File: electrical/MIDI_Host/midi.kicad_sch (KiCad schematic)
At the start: 35 parts, among them U1 BL1551B, U2 BL1551B, U3 BL1551B, U4 BL1551B, U5 74HC1G14GV, U6 6N137, U7 6N137

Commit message: SUKU sch done
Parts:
- removed C1, C3, C5, C8: 100n, suku_basics:CAP_0805, symbol suku_basics:CAP
- removed C7: 100u, suku_basics:CAP_0805, symbol suku_basics:CAP
- removed D1, D2, D3, D4, D6: 1N4148WT, Diode_SMD:D_SOD-523, symbol suku_basics:SCHOTTKY
- removed D5: 5V1, Diode_SMD:D_SOD-523, symbol suku_basics:ZENER
- removed TP1: +RECT, TestPoint:TestPoint_THTPad_1.0x1.0mm_Drill0.5mm, symbol Connector:TestPoint_Alt
- removed TP2: -RECT, TestPoint:TestPoint_THTPad_1.0x1.0mm_Drill0.5mm, symbol Connector:TestPoint_Alt
- removed TP4: INV_RX, TestPoint:TestPoint_THTPad_1.0x1.0mm_Drill0.5mm, symbol Connector:TestPoint_Alt
- removed U4: BL1551B, suku_basics:SOT-23-5-AND-TSSOP5, symbol suku_basics:BL1551B
- added R15: (no value), suku_basics:RES_0805, symbol suku_basics:RES
- R4: value 470R -> 350R
- R5: value 350R -> (none)
- U1, U2, U3: value BL1551B -> (none); footprint suku_basics:SOT-23-5-AND-TSSOP5 -> suku_basics:SOT-363_SC-70-6
- U6, U7: value 6N137 -> (none); footprint suku_basics:OPTO_SMD-8_L9.8-W6.6-P2.54-LS10.3-BL -> (none)
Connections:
- net VCOM is gone; now on net GND: U3.2 (GND), U7.5 (GND)
- net +5V: now also R4.1, U3.5 (VCC), U7.7 (EN), U7.8 (VCC)
- net GND: now also R15.2; no longer U7.3 (C)
- net INVERTED_UART_MIDI_RX: now also R5.1, R15.1; no longer R6.2, U6.6 (VO)
- net TRS_TYPE_A: now also U3.6 (ENB); no longer R4.2
- net at U6.2 (A): now also Audio1.3, U7.3 (C); no longer R3.2
- net at U6.3 (C): now also R3.1, U7.2 (A); no longer U3.1 (A1)
- net at Audio1.2: now also R3.2
- net at U3.4 (B): now also R5.2; no longer Audio1.3
- net at U3.3 (A2): now also R4.2, U7.6 (VO); no longer R3.1
- removed net VBUS: R5.1, U3.5 (VCC), U7.7 (EN), U7.8 (VCC)
- new net: R6.2, U3.1 (A1), U6.6 (VO)
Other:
- moved on the sheet: C6, C9, R3, R6, TP5, U6, U7

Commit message: SUKU sync
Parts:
- R15, R5: value (none) -> RES
- U1, U2, U3: value (none) -> BL1551B
- U6, U7: value (none) -> 6N137; footprint (none) -> suku_basics:OPTO_SMD-8_L9.8-W6.6-P2.54-LS10.3-BL
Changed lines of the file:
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@@
       (effects (font (size 1.27 1.27)) hide)
     )
-    (property "Value" "" (id 1) (at 160.02 83.82 0))
+    (property "Value" "+5V" (id 1) (at 160.02 83.82 0))
     (property "Footprint" "" (id 2) (at 160.02 88.9 0)
       (effects (font (size 1.27 1.27)) hide)
@@
     (in_bom yes) (on_board yes) (fields_autoplaced)
     (property "Reference" "U7" (id 0) (at 99.06 96.52 0))
-    (property "Value" "" (id 1) (at 99.06 99.06 0))
-    (property "Footprint" "" (id 2) (at 99.06 121.92 0)
+    (property "Value" "6N137" (id 1) (at 99.06 99.06 0))
+    (property "Footprint" "suku_basics:OPTO_SMD-8_L9.8-W6.6-P2.54-LS10.3-BL" (id 2) (at 99.06 121.92 0)
       (effects (font (size 1.27 1.27)) hide)
     )
@@
     (in_bom yes) (on_board yes)
     (property "Reference" "U1" (id 0) (at 83.82 146.05 0))
-    (property "Value" "" (id 1) (at 83.82 148.59 0))
+    (property "Value" "BL1551B" (id 1) (at 83.82 148.59 0))
     (property "Footprint" "suku_basics:SOT-363_SC-70-6" (id 2) (at 83.82 165.1 0)
       (effects (font (size 1.27 1.27)) hide)
@@
     (in_bom yes) (on_board yes)
     (property "Reference" "U3" (id 0) (at 149.86 87.63 0))
-    (property "Value" "" (id 1) (at 149.86 90.17 0))
+    (property "Value" "BL1551B" (id 1) (at 149.86 90.17 0))
     (property "Footprint" "suku_basics:SOT-363_SC-70-6" (id 2) (at 149.86 106.68 0)
       (effects (font (size 1.27 1.27)) hide)
@@
       (effects (font (size 1.27 1.27)) hide)
     )
-    (property "Value" "" (id 1) (at 165.1 124.46 0))
+    (property "Value" "GND" (id 1) (at 165.1 124.46 0))
     (property "Footprint" "" (id 2) (at 165.1 119.38 0)
       (effects (font (size 1.27 1.27)) hide)
@@
       (effects (font (size 1.27 1.27)) (justify left))
     )
-    (property "Value" "" (id 1) (at 167.64 115.5699 0)
+    (property "Value" "RES" (id 1) (at 167.64 115.5699 0)
       (effects (font (size 1.27 1.27)) (justify left))
     )
@@
     (in_bom yes) (on_board yes) (fields_autoplaced)
     (property "Reference" "U2" (id 0) (at 83.82 163.83 0))
-    (property "Value" "" (id 1) (at 83.82 166.37 0))
+    (property "Value" "BL1551B" (id 1) (at 83.82 166.37 0))
     (property "Footprint" "suku_basics:SOT-363_SC-70-6" (id 2) (at 83.82 182.88 0)
       (effects (font (size 1.27 1.27)) hide)
@@
     (in_bom yes) (on_board yes) (fields_autoplaced)
     (property "Reference" "U6" (id 0) (at 99.06 68.58 0))
-    (property "Value" "" (id 1) (at 99.06 71.12 0))
-    (property "Footprint" "" (id 2) (at 99.06 93.98 0)
+    (property "Value" "6N137" (id 1) (at 99.06 71.12 0))
+    (property "Footprint" "suku_basics:OPTO_SMD-8_L9.8-W6.6-P2.54-LS10.3-BL" (id 2) (at 99.06 93.98 0)
       (effects (font (size 1.27 1.27)) hide)
     )
@@
       (effects (font (size 1.27 1.27)) hide)
     )
-    (property "Value" "" (id 1) (at 139.7 106.68 0))
+    (property "Value" "GND" (id 1) (at 139.7 106.68 0))
     (property "Footprint" "" (id 2) (at 139.7 101.6 0)
       (effects (font (size 1.27 1.27)) hide)
@@
       (effects (font (size 1.27 1.27)) (justify right))
     )
-    (property "Value" "" (id 1) (at 167.64 105.4099 0)
+    (property "Value" "RES" (id 1) (at 167.64 105.4099 0)
       (effects (font (size 1.27 1.27)) (justify right))
     )

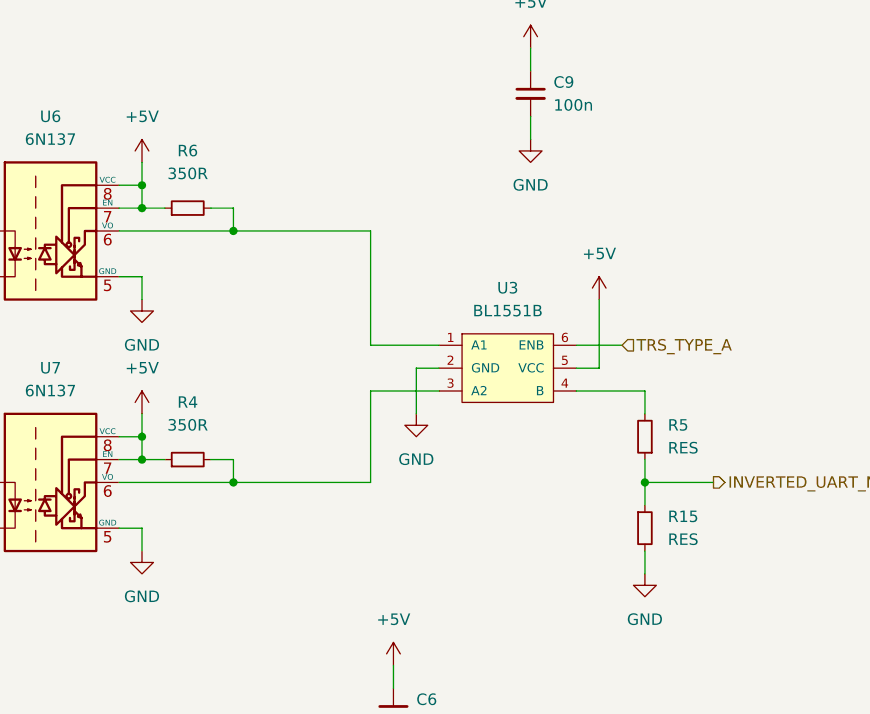
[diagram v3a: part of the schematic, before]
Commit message: SUKU resistor values added
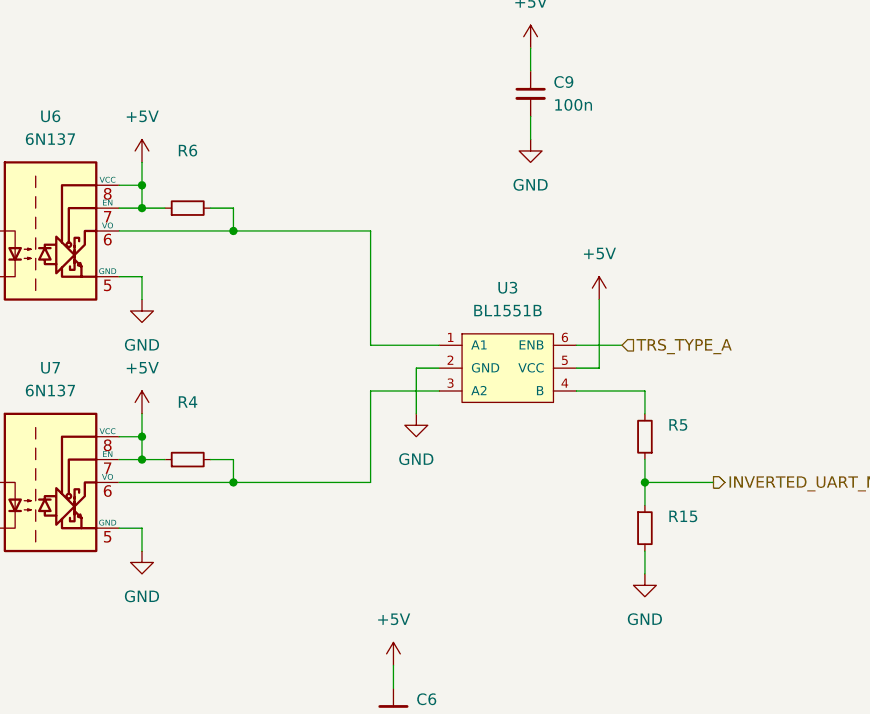
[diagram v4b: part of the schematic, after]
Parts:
- R15, R5: value RES -> (none); footprint suku_basics:RES_0805 -> (none)
- R4: value 350R -> (none)
- R6: value 350R -> (none); footprint suku_basics:RES_0805 -> (none)
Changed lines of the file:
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@@
       (effects (font (size 1.27 1.27)) (justify left))
     )
-    (property "Value" "RES" (id 1) (at 167.64 115.5699 0)
+    (property "Value" "" (id 1) (at 167.64 115.5699 0)
       (effects (font (size 1.27 1.27)) (justify left))
     )
-    (property "Footprint" "suku_basics:RES_0805" (id 2) (at 165.1 114.3 0)
+    (property "Footprint" "" (id 2) (at 165.1 114.3 0)
       (effects (font (size 1.27 1.27)) hide)
     )
@@
     (in_bom yes) (on_board yes) (fields_autoplaced)
     (property "Reference" "R4" (id 0) (at 114.3 100.33 90))
-    (property "Value" "350R" (id 1) (at 114.3 102.87 90))
+    (property "Value" "" (id 1) (at 114.3 102.87 90))
     (property "Footprint" "suku_basics:RES_0805" (id 2) (at 114.3 106.68 0)
       (effects (font (size 1.27 1.27)) hide)
@@
     (in_bom yes) (on_board yes) (fields_autoplaced)
     (property "Reference" "R6" (id 0) (at 114.3 72.39 90))
-    (property "Value" "350R" (id 1) (at 114.3 74.93 90))
-    (property "Footprint" "suku_basics:RES_0805" (id 2) (at 114.3 78.74 0)
+    (property "Value" "" (id 1) (at 114.3 74.93 90))
+    (property "Footprint" "" (id 2) (at 114.3 78.74 0)
       (effects (font (size 1.27 1.27)) hide)
     )
@@
       (effects (font (size 1.27 1.27)) (justify right))
     )
-    (property "Value" "RES" (id 1) (at 167.64 105.4099 0)
+    (property "Value" "" (id 1) (at 167.64 105.4099 0)
       (effects (font (size 1.27 1.27)) (justify right))
     )
-    (property "Footprint" "suku_basics:RES_0805" (id 2) (at 165.1 104.14 0)
+    (property "Footprint" "" (id 2) (at 165.1 104.14 0)
       (effects (font (size 1.27 1.27)) hide)
     )

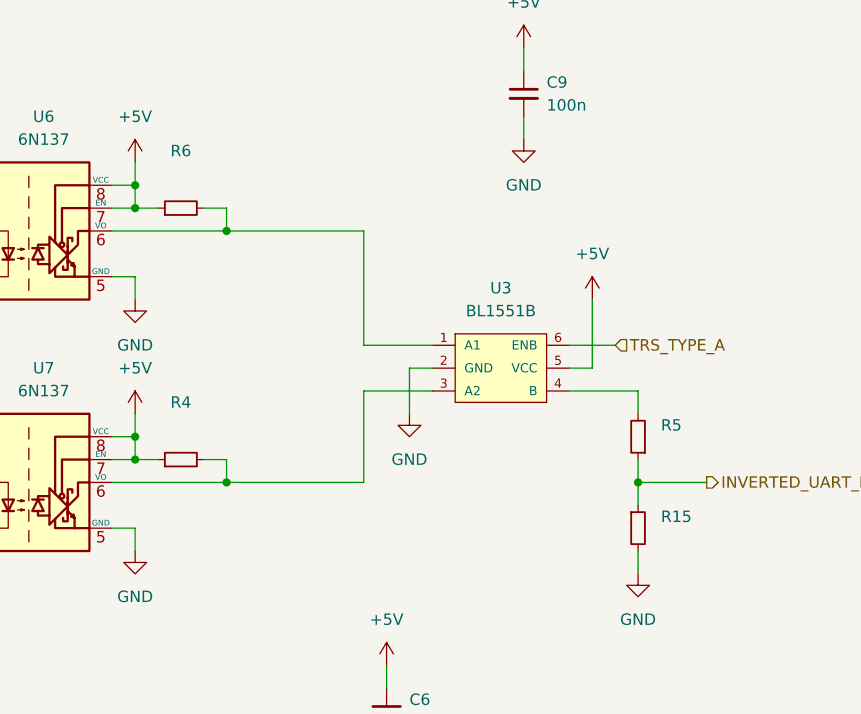
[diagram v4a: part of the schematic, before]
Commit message: SUKU mechanical exports added
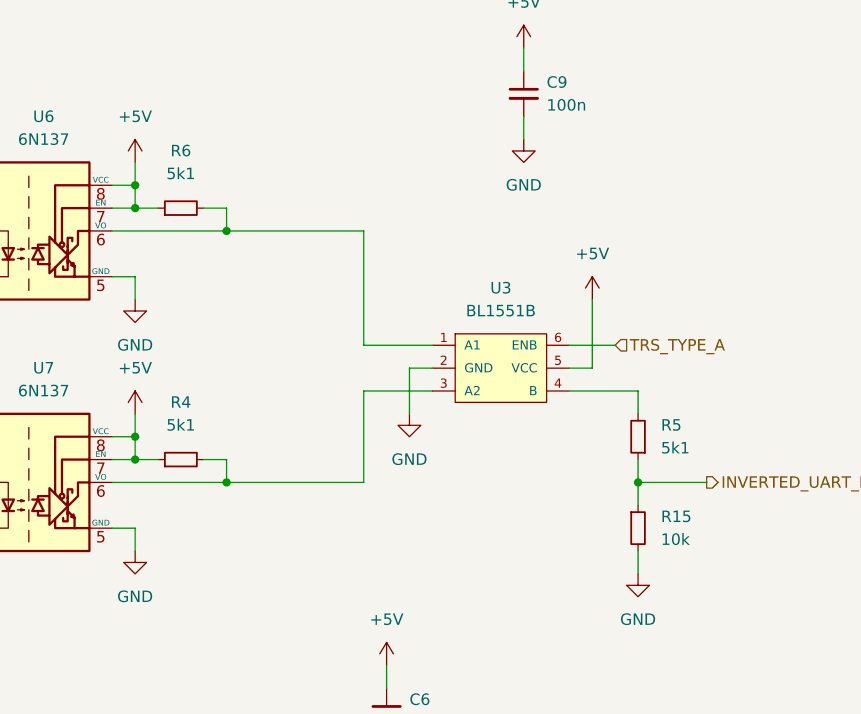
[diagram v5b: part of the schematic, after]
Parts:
- R15: value (none) -> 10k; footprint (none) -> suku_basics:RES_0805
- R4: value (none) -> 5k1
- R5, R6: value (none) -> 5k1; footprint (none) -> suku_basics:RES_0805
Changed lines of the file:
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@@
       (effects (font (size 1.27 1.27)) (justify left))
     )
-    (property "Value" "" (id 1) (at 167.64 115.5699 0)
+    (property "Value" "10k" (id 1) (at 167.64 115.5699 0)
       (effects (font (size 1.27 1.27)) (justify left))
     )
-    (property "Footprint" "" (id 2) (at 165.1 114.3 0)
+    (property "Footprint" "suku_basics:RES_0805" (id 2) (at 165.1 114.3 0)
       (effects (font (size 1.27 1.27)) hide)
     )
@@
     (in_bom yes) (on_board yes) (fields_autoplaced)
     (property "Reference" "R4" (id 0) (at 114.3 100.33 90))
-    (property "Value" "" (id 1) (at 114.3 102.87 90))
+    (property "Value" "5k1" (id 1) (at 114.3 102.87 90))
     (property "Footprint" "suku_basics:RES_0805" (id 2) (at 114.3 106.68 0)
       (effects (font (size 1.27 1.27)) hide)
@@
     (in_bom yes) (on_board yes) (fields_autoplaced)
     (property "Reference" "R6" (id 0) (at 114.3 72.39 90))
-    (property "Value" "" (id 1) (at 114.3 74.93 90))
-    (property "Footprint" "" (id 2) (at 114.3 78.74 0)
+    (property "Value" "5k1" (id 1) (at 114.3 74.93 90))
+    (property "Footprint" "suku_basics:RES_0805" (id 2) (at 114.3 78.74 0)
       (effects (font (size 1.27 1.27)) hide)
     )
@@
       (effects (font (size 1.27 1.27)) (justify right))
     )
-    (property "Value" "" (id 1) (at 167.64 105.4099 0)
+    (property "Value" "5k1" (id 1) (at 167.64 105.4099 0)
       (effects (font (size 1.27 1.27)) (justify right))
     )
-    (property "Footprint" "" (id 2) (at 165.1 104.14 0)
+    (property "Footprint" "suku_basics:RES_0805" (id 2) (at 165.1 104.14 0)
       (effects (font (size 1.27 1.27)) hide)
     )

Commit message: SUKU pcb revision done
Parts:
- removed TP3: INV_TX, TestPoint:TestPoint_THTPad_1.0x1.0mm_Drill0.5mm, symbol Connector:TestPoint_Alt
- removed TP5: TYPE_A, TestPoint:TestPoint_THTPad_1.0x1.0mm_Drill0.5mm, symbol Connector:TestPoint_Alt
- added TP17, TP18, TP19, TP20, TP21: (no value), symbol Connector:TestPoint_Alt
- added TP22: G, TestPoint:TestPoint_THTPad_1.0x1.0mm_Drill0.5mm, symbol Connector:TestPoint_Alt
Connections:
- net GND: now also TP19.1, TP22.1
- net OUT_R: now reaches Audio2.2, R2.1
- net OUT_R: now also TP21.1
- net OUT_T: now reaches Audio2.3, R1.1
- net OUT_T: now also TP20.1
- net IN_T: now reaches Audio1.3, U6.2 (A), U7.3 (C)
- net IN_T: now also TP17.1
- net IN_R: now reaches Audio1.2, R3.2
- net IN_R: now also TP18.1
- net INVERTED_UART_MIDI_RX renamed RX
- net INVERTED_UART_MIDI_TX renamed TX
- net TRS_TYPE_A renamed TX_AB_SELECT
- net TX_AB_SELECT: no longer U3.6 (ENB)
- new net RX_AB_SELECT: U3.6 (ENB)
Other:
- moved on the sheet: Audio2

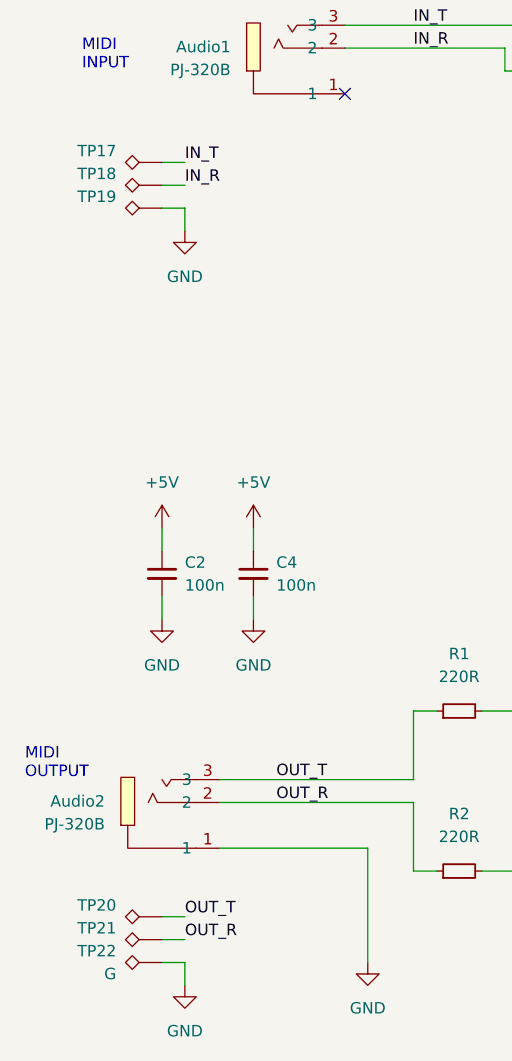
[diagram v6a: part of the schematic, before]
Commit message: SUKU capacitor footprint fixed,packup placement added
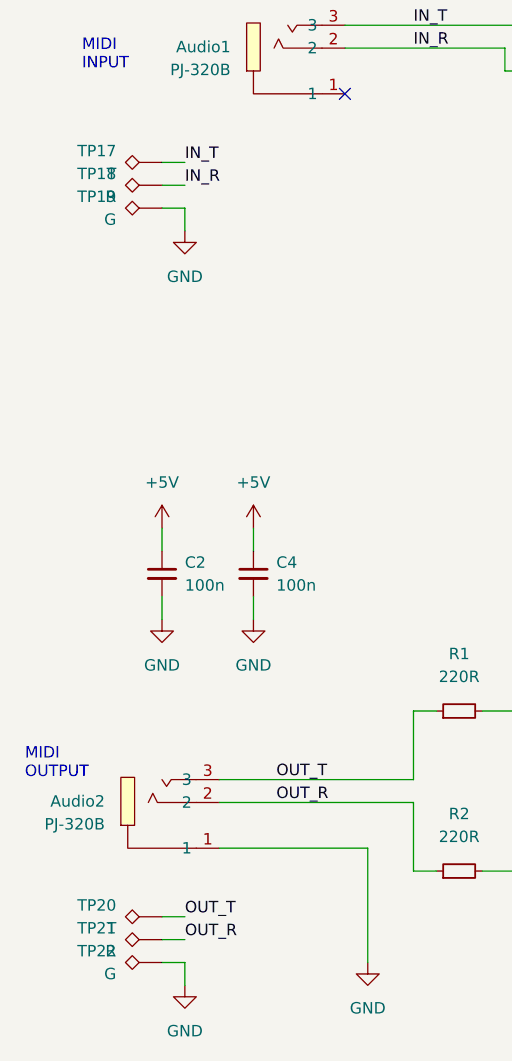
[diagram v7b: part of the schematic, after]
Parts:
- TP17, TP20: value (none) -> T; footprint (none) -> TestPoint:TestPoint_THTPad_D1.0mm_Drill0.5mm
- TP18, TP21: value (none) -> R; footprint (none) -> TestPoint:TestPoint_THTPad_D1.0mm_Drill0.5mm
- TP19: value (none) -> G; footprint (none) -> TestPoint:TestPoint_THTPad_1.0x1.0mm_Drill0.5mm
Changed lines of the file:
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@@
       (effects (font (size 1.27 1.27)) (justify left))
     )
-    (property "Value" "" (id 1) (at 25.4 97.7899 90)
-      (effects (font (size 1.27 1.27)) (justify left))
-    )
-    (property "Footprint" "" (id 2) (at 30.48 101.6 0)
+    (property "Value" "T" (id 1) (at 25.4 97.7899 90)
+      (effects (font (size 1.27 1.27)) (justify left))
+    )
+    (property "Footprint" "TestPoint:TestPoint_THTPad_D1.0mm_Drill0.5mm" (id 2) (at 30.48 101.6 0)
       (effects (font (size 1.27 1.27)) hide)
     )
@@
       (effects (font (size 1.27 1.27)) (justify left))
     )
-    (property "Value" "" (id 1) (at 25.4 100.3299 90)
-      (effects (font (size 1.27 1.27)) (justify left))
-    )
-    (property "Footprint" "" (id 2) (at 30.48 104.14 0)
+    (property "Value" "R" (id 1) (at 25.4 100.3299 90)
+      (effects (font (size 1.27 1.27)) (justify left))
+    )
+    (property "Footprint" "TestPoint:TestPoint_THTPad_D1.0mm_Drill0.5mm" (id 2) (at 30.48 104.14 0)
       (effects (font (size 1.27 1.27)) hide)
     )
@@
       (effects (font (size 1.27 1.27)) (justify left))
     )
-    (property "Value" "" (id 1) (at 25.4 102.8699 90)
-      (effects (font (size 1.27 1.27)) (justify left))
-    )
-    (property "Footprint" "" (id 2) (at 30.48 106.68 0)
+    (property "Value" "G" (id 1) (at 25.4 102.8699 90)
+      (effects (font (size 1.27 1.27)) (justify left))
+    )
+    (property "Footprint" "TestPoint:TestPoint_THTPad_1.0x1.0mm_Drill0.5mm" (id 2) (at 30.48 106.68 0)
       (effects (font (size 1.27 1.27)) hide)
     )
@@
       (effects (font (size 1.27 1.27)) (justify left))
     )
-    (property "Value" "" (id 1) (at 25.4 184.1499 90)
-      (effects (font (size 1.27 1.27)) (justify left))
-    )
-    (property "Footprint" "" (id 2) (at 30.48 187.96 0)
+    (property "Value" "R" (id 1) (at 25.4 184.1499 90)
+      (effects (font (size 1.27 1.27)) (justify left))
+    )
+    (property "Footprint" "TestPoint:TestPoint_THTPad_D1.0mm_Drill0.5mm" (id 2) (at 30.48 187.96 0)
       (effects (font (size 1.27 1.27)) hide)
     )
@@
       (effects (font (size 1.27 1.27)) (justify left))
     )
-    (property "Value" "" (id 1) (at 25.4 181.6099 90)
-      (effects (font (size 1.27 1.27)) (justify left))
-    )
-    (property "Footprint" "" (id 2) (at 30.48 185.42 0)
-      (effects (font (size 1.27 1.27)) hide)
-    )
+    (property "Value" "T" (id 1) (at 25.4 181.6099 90)
+      (effects (font (size 1.27 1.27)) (justify left))
+    )
+    (property "Footprint" "TestPoint:TestPoint_THTPad_D1.0mm_Drill0.5mm" (id 2) (at 30.48 185.42 0)
+      (effects (font (size 1.27 1.27)) hide)
+    )
